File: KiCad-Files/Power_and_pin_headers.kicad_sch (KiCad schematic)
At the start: 47 parts, among them J4 CON-SOCJ-2155, J5 Conn_01x04, J6 Conn_01x05, U4 MIC2099-1YMT-TR, U5 AP2114HA-1.2TRG1, U6 AZ1117CH2-3.3TRG1, U7 MIC2099-1YMT-TR

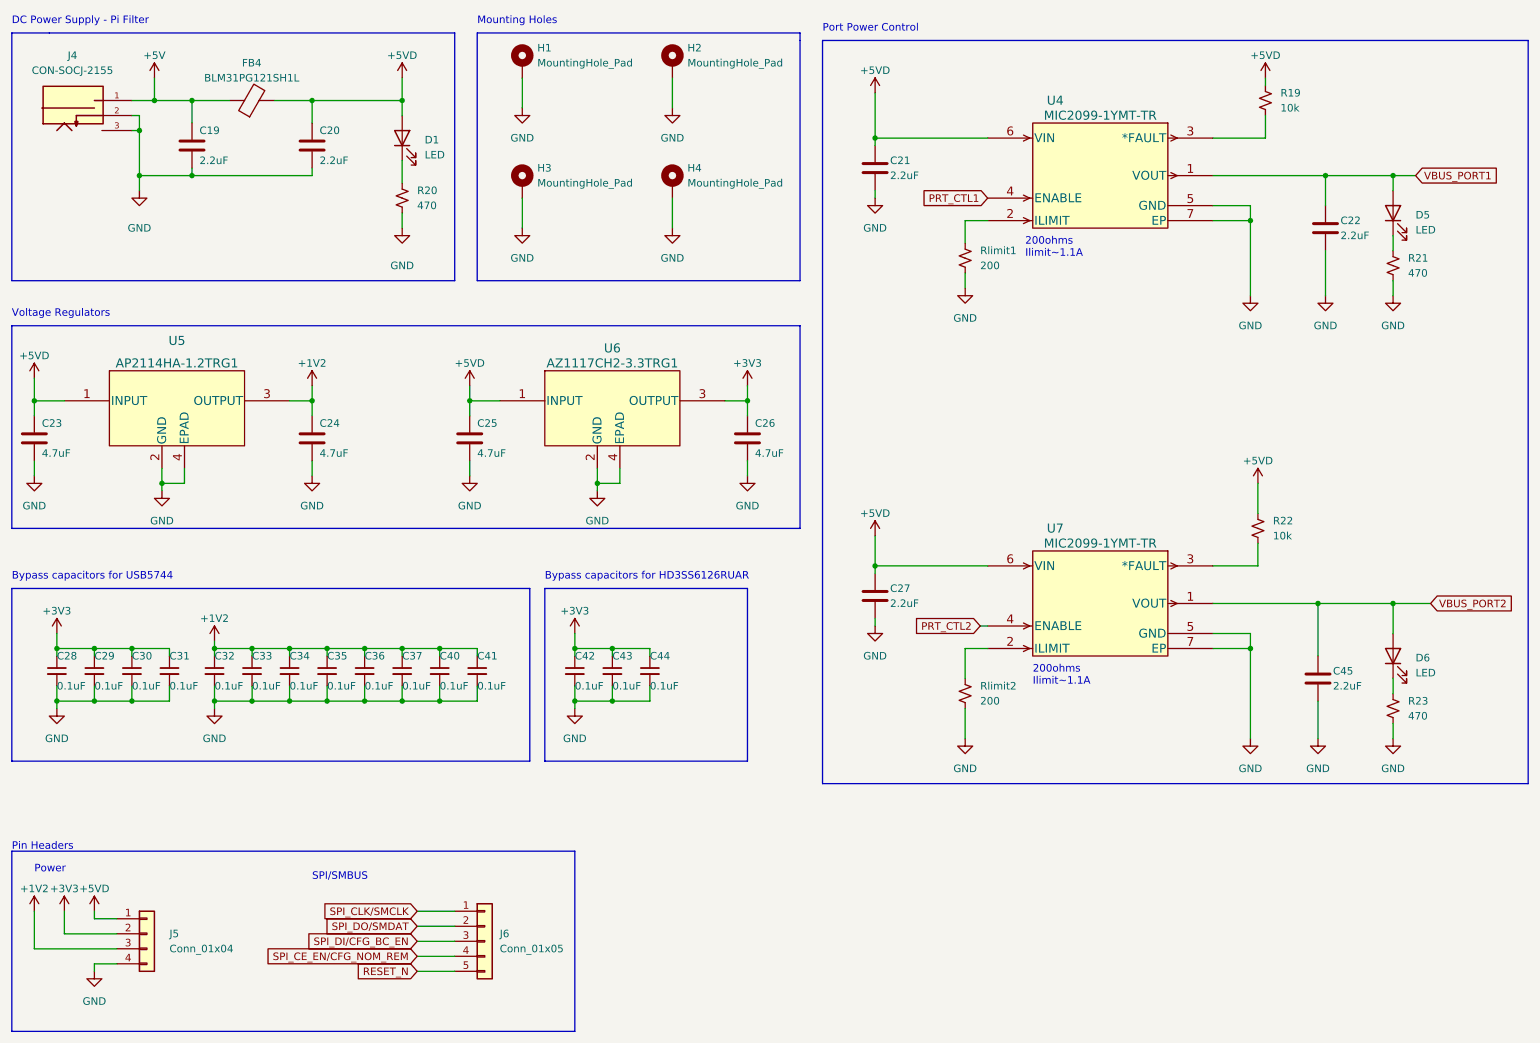
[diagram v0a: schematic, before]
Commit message: Added silkscreen and made power planes a bit wider
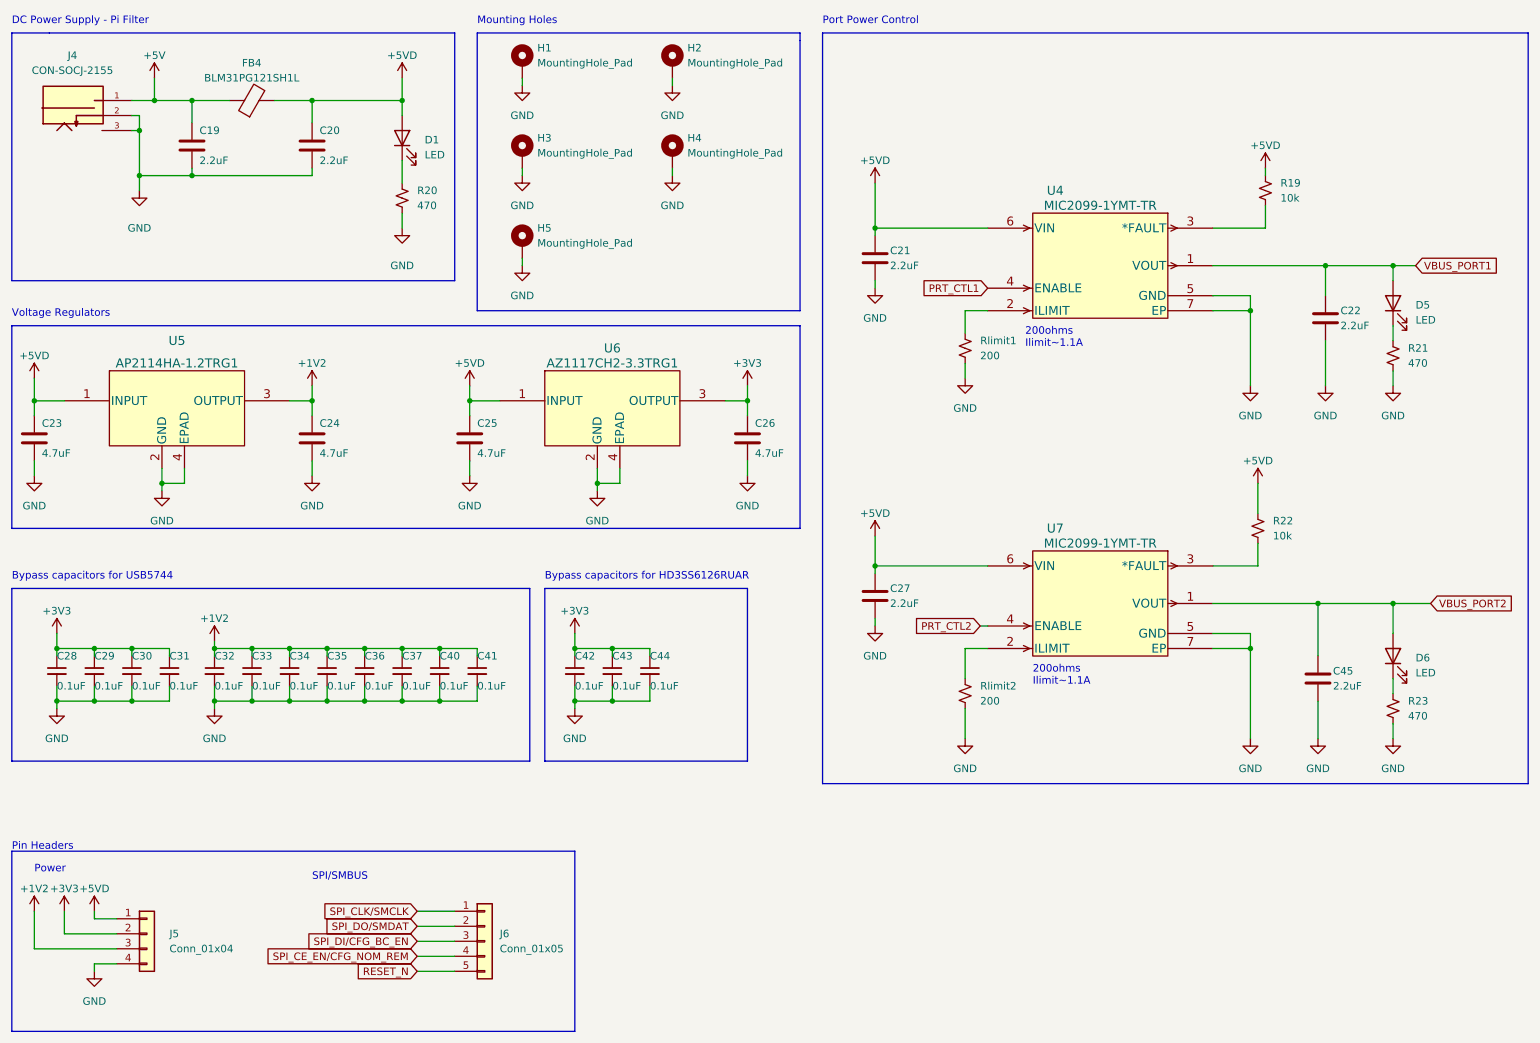
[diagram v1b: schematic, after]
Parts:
- added H5: MountingHole_Pad, MountingHole:MountingHole_3mm_Pad_Via, symbol Mechanical:MountingHole_Pad
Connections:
- net GND: now also H5.1
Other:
- moved on the sheet: C21, C22, D5, H3, H4, R19, R21, Rlimit1, U4
